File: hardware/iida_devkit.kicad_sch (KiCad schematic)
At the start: 4 parts

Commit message: HW: Refine schematic
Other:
- sheet Power ports: added V_3V3, V_BAT; removed +3.3V, V_{BAT}
- note added: "This is a project for practicing PCB design and programming. The result is a device that is powered either with a battery or with a USB connection. The device can recharge the battery via the USB connection. The device includes: - An example sensor (temperature) - External flash for updating the firmware over the air (FOTA) - A modem module that connects the main microcontroller to the internet w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"
- note removed: "This is a project for practicing PCB design and programming. The result is a device that is powered either with a battery or with a USB connection. The device can recharge the batteries via the USB connection. The device includes: - An example sensor (temperature) - External flash for updating the firmware over the air (FOTA) - A modem module that connects the main microcontroller to the internet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"
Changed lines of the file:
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@@
+	(wire
+		(pts
+			(xy 151.13 105.41) (xy 142.24 105.41)
+		)
+		(stroke
+			(width 0)
+			(type default)
+		)
+	)
 	(wire
 		(pts
@@
 	(wire
 		(pts
-			(xy 142.24 105.41) (xy 149.86 105.41)
-		)
-		(stroke
-			(width 0)
-			(type default)
-		)
-	)
-	(wire
-		(pts
 			(xy 142.24 102.87) (xy 144.78 102.87)
 		)
@@
 		(pts
 			(xy 118.11 128.27) (xy 124.46 128.27)
+		)
+		(stroke
+			(width 0)
+			(type default)
+		)
+	)
+	(wire
+		(pts
+			(xy 151.13 102.87) (xy 151.13 105.41)
 		)
 		(stroke
@@
 		)
 	)
-	(text "This is a project for practicing PCB design and programming.\n\nThe result is a device that is powered either with a battery or with a USB connection.\nThe device can recharge the batteries via the USB connection.\n\nThe device includes:\n  - An example sensor (temperature)\n  - External flash for updating the firmware over the air (FOTA)\n  - A modem module that connects the main microcontroller to the internet with LTE CAT-M1\n  - Option to use either an external antenna or an integrated antenna\n\nA key goal of the project is to ensure it has as little reliance as possible on totalitarian\ncountries like China or Russia.\nComponent sourcing must be done carefully to select manufacturers who can supply parts that are not\nproduced in such countries.\nInstead, democratic countries such as Taiwan and Germany should be preferred.\n\nTo reduce strain on the global environment, manufacturing and sourcing is centered around Europe."
+	(text "This is a project for practicing PCB design and programming.\n\nThe result is a device that is powered either with a battery or with a USB connection.\nThe device can recharge the battery via the USB connection.\n\nThe device includes:\n  - An example sensor (temperature)\n  - External flash for updating the firmware over the air (FOTA)\n  - A modem module that connects the main microcontroller to the internet with LTE CAT-M1\n  - Option to use either an external antenna or an integrated antenna\n\nA key goal of the project is to ensure it has as little reliance as possible on totalitarian\ncountries (e.g., China or Russia) or on hostile countries (e.g., USA).\nComponent sourcing must be done carefully to select manufacturers who can supply parts that are not\nproduced in such countries.\nInstead, democratic countries (e.g., Taiwan and Germany) should be preferred.\n\nTo reduce strain on the global environment, manufacturing and sourcing is centered around Europe."
 		(exclude_from_sim no)
 		(at 14.478 52.07 0)
@@
 		(dnp no)
 		(fields_autoplaced yes)
-		(property "Reference" "#PWR03"
+		(property "Reference" "#PWR02"
 			(at 149.86 198.12 0)
 			(effects
@@
 			(project "iida_devkit"
 				(path "/b12a6e25-97fb-4aba-bc96-af8db389bb9a"
-					(reference "#PWR03")
+					(reference "#PWR02")
+					(unit 1)
+				)
+			)
+		)
+	)
+	(symbol
+		(lib_id "power:+3.3V")
+		(at 144.78 102.87 0)
+		(unit 1)
+		(exclude_from_sim no)
+		(in_bom yes)
+		(on_board yes)
+		(dnp no)
+		(property "Reference" "#PWR01"
+			(at 144.78 106.68 0)
+			(effects
+				(font
+					(size 1.27 1.27)
+				)
+				(hide yes)
+			)
+		)
+		(property "Value" "V_3V3"
+			(at 144.78 99.314 0)
+			(effects
+				(font
+					(size 1.27 1.27)
+				)
+			)
+		)
+		(property "Footprint" ""
+			(at 144.78 102.87 0)
+			(effects
+				(font
+					(size 1.27 1.27)
+				)
+				(hide yes)
+			)
+		)
+		(property "Datasheet" ""
+			(at 144.78 102.87 0)
+			(effects
+				(font
+					(size 1.27 1.27)
+				)
+				(hide yes)
+			)
+		)
+		(property "Description" "Power symbol creates a global label with name \"+3.3V\""
+			(at 144.78 102.87 0)
+			(effects
+				(font
+					(size 1.27 1.27)
+				)
+				(hide yes)
+			)
+		)
+		(pin "1"
+		)
+		(instances
+			(project "iida_devkit"
+				(path "/b12a6e25-97fb-4aba-bc96-af8db389bb9a"
+					(reference "#PWR01")
 					(unit 1)
 				)
@@
 	(symbol
 		(lib_id "power:+BATT")
-		(at 149.86 105.41 0)
+		(at 151.13 102.87 0)
 		(unit 1)
 		(exclude_from_sim no)
@@
 		(on_board yes)
 		(dnp no)
-		(property "Reference" "#PWR02"
-			(at 149.86 109.22 0)
-			(effects
-				(font
-					(size 1.27 1.27)
-				)
-				(hide yes)
-			)
-		)
-		(property "Value" "+VBAT"
-			(at 149.86 101.854 0)
+		(property "Reference" "#PWR03"
+			(at 151.13 106.68 0)
+			(effects
+				(font
+					(size 1.27 1.27)
+				)
+				(hide yes)
+			)
+		)
+		(property "Value" "V_BAT"
+			(at 151.13 99.314 0)
 			(effects
 				(font
@@
 		)
 		(property "Footprint" ""
-			(at 149.86 105.41 0)
+			(at 151.13 102.87 0)
 			(effects
 				(font
@@
 		)
 		(property "Datasheet" ""
-			(at 149.86 105.41 0)
+			(at 151.13 102.87 0)
 			(effects
 				(font
@@
 		)
 		(property "Description" "Power symbol creates a global label with name \"+BATT\""
-			(at 149.86 105.41 0)
+			(at 151.13 102.87 0)
 			(effects
 				(font
@@
 			(project "iida_devkit"
 				(path "/b12a6e25-97fb-4aba-bc96-af8db389bb9a"
-					(reference "#PWR02")
-					(unit 1)
-				)
-			)
-		)
-	)
-	(symbol
-		(lib_id "power:+3.3V")
-		(at 144.78 102.87 0)
-		(unit 1)
-		(exclude_from_sim no)
-		(in_bom yes)
-		(on_board yes)
-		(dnp no)
-		(property "Reference" "#PWR01"
-			(at 144.78 106.68 0)
-			(effects
-				(font
-					(size 1.27 1.27)
-				)
-				(hide yes)
-			)
-		)
-		(property "Value" "+3.3V"
-			(at 144.78 99.06 0)
-			(effects
-				(font
-					(size 1.27 1.27)
-				)
-			)
-		)
-		(property "Footprint" ""
-			(at 144.78 102.87 0)
-			(effects
-				(font
-					(size 1.27 1.27)
-				)
-				(hide yes)
-			)
-		)
-		(property "Datasheet" ""
-			(at 144.78 102.87 0)
-			(effects
-				(font
-					(size 1.27 1.27)
-				)
-				(hide yes)
-			)
-		)
-		(property "Description" "Power symbol creates a global label with name \"+3.3V\""
-			(at 144.78 102.87 0)
-			(effects
-				(font
-					(size 1.27 1.27)
-				)
-				(hide yes)
-			)
-		)
-		(pin "1"
-		)
-		(instances
-			(project "iida_devkit"
-				(path "/b12a6e25-97fb-4aba-bc96-af8db389bb9a"
-					(reference "#PWR01")
+					(reference "#PWR03")
 					(unit 1)
 				)
@@
 			)
 		)
-		(pin "V_{BAT}" output
+		(pin "V_BAT" output
 			(at 142.24 105.41 0)
 			(effects
@@
 			)
 		)
-		(pin "+3.3V" output
+		(pin "V_3V3" output
 			(at 142.24 102.87 0)
 			(effects

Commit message: HW: Start working on Hw v5.0.0
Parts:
- H1, H2, H3, H4: Digi-Key Part Number - -> (none)
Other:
- added sheet Antenna (antenna.kicad_sch)
- added sheet Battery (battery.kicad_sch)
- added sheet USB (usb.kicad_sch)
- sheet MCU ports: added MDM_PWR_EN, MDM_PWR_ON, MDM_RESET, MDM_RXD, MDM_TXD, V_BAT; removed MODEM_PWR_ENn, MODEM_RESET, MODEM_RX, MODEM_TX
- sheet Modem ports: added ANT, MDM_PWR_EN, MDM_PWR_ON, MDM_RESET, MDM_RXD, MDM_TXD, MDM_V_INT, SIM_DET, SIM_VCC; removed MODEM_PWR_ENn, MODEM_RESET, MODEM_RX, MODEM_TX, VSIM
- sheet Power ports: added V_5V0; removed USB_DN, USB_DP
- sheet SIM ports: added MDM_V_INT, SIM_DET, SIM_VCC; removed VSIM

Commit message: HW: Refine schematic
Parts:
- H1, H2, H3, H4: footprint MountingHole:MountingHole_2.2mm_M2_Pad_Via -> MountingHole:MountingHole_5.3mm_M5_Pad_Via
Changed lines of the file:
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@@
 			)
 		)
-		(property "Footprint" "MountingHole:MountingHole_2.2mm_M2_Pad_Via"
+		(property "Footprint" "MountingHole:MountingHole_5.3mm_M5_Pad_Via"
 			(at 134.62 189.23 0)
 			(effects
@@
 			)
 		)
-		(property "Footprint" "MountingHole:MountingHole_2.2mm_M2_Pad_Via"
+		(property "Footprint" "MountingHole:MountingHole_5.3mm_M5_Pad_Via"
 			(at 149.86 189.23 0)
 			(effects
@@
 			)
 		)
-		(property "Footprint" "MountingHole:MountingHole_2.2mm_M2_Pad_Via"
+		(property "Footprint" "MountingHole:MountingHole_5.3mm_M5_Pad_Via"
 			(at 139.7 189.23 0)
 			(effects
@@
 			)
 		)
-		(property "Footprint" "MountingHole:MountingHole_2.2mm_M2_Pad_Via"
+		(property "Footprint" "MountingHole:MountingHole_5.3mm_M5_Pad_Via"
 			(at 144.78 189.23 0)
 			(effects

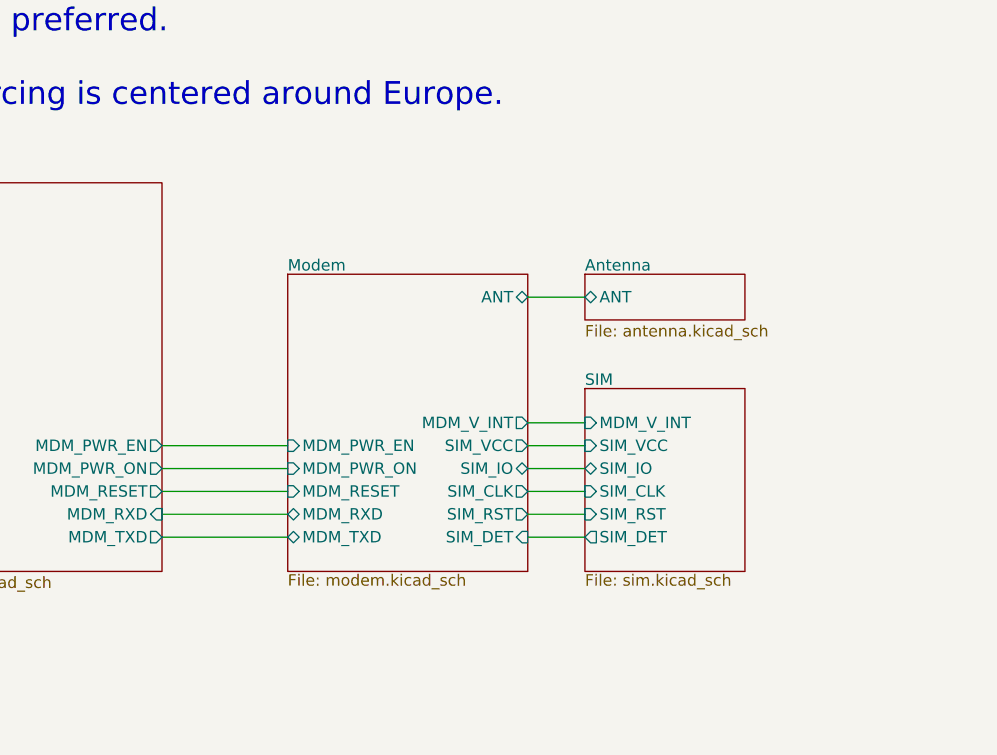
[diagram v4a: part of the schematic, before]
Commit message: HW: Fill BOM and refine schema
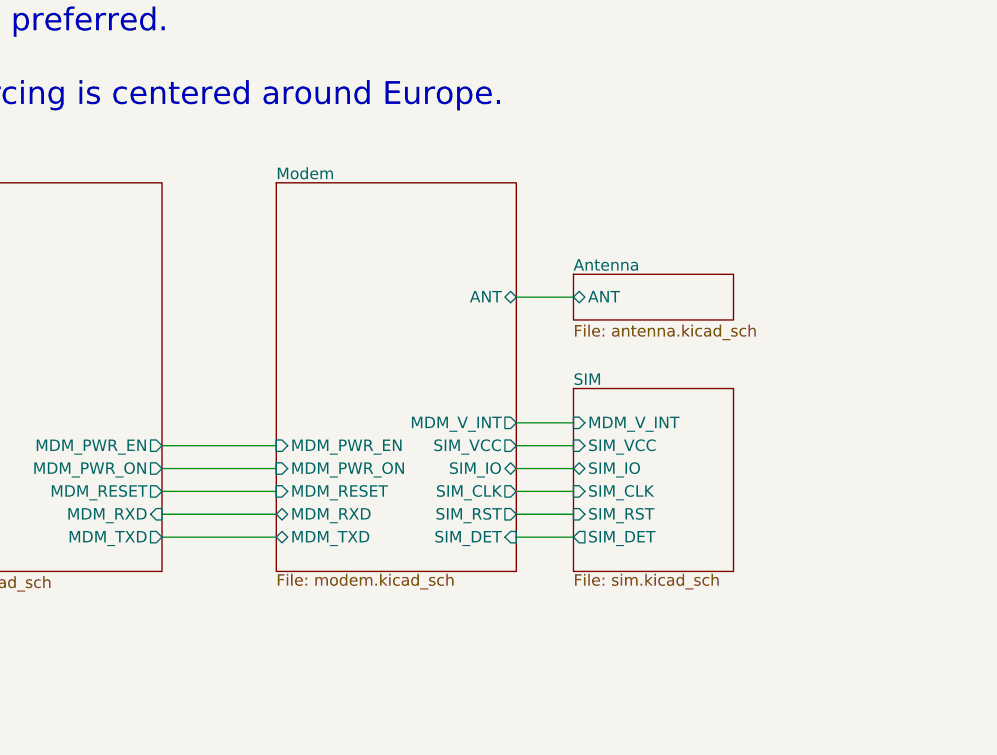
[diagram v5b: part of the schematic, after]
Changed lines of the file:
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@@
 	(wire
 		(pts
-			(xy 193.04 128.27) (xy 199.39 128.27)
-		)
-		(stroke
-			(width 0)
-			(type default)
-		)
-	)
-	(wire
-		(pts
-			(xy 193.04 135.89) (xy 199.39 135.89)
-		)
-		(stroke
-			(width 0)
-			(type default)
-		)
-	)
-	(wire
-		(pts
-			(xy 152.4 133.35) (xy 166.37 133.35)
+			(xy 191.77 128.27) (xy 198.12 128.27)
+		)
+		(stroke
+			(width 0)
+			(type default)
+		)
+	)
+	(wire
+		(pts
+			(xy 191.77 135.89) (xy 198.12 135.89)
+		)
+		(stroke
+			(width 0)
+			(type default)
+		)
+	)
+	(wire
+		(pts
+			(xy 152.4 133.35) (xy 165.1 133.35)
 		)
 		(stroke
@@
 	(wire
 		(pts
-			(xy 152.4 130.81) (xy 166.37 130.81)
-		)
-		(stroke
-			(width 0)
-			(type default)
-		)
-	)
-	(wire
-		(pts
-			(xy 193.04 133.35) (xy 199.39 133.35)
+			(xy 152.4 130.81) (xy 165.1 130.81)
+		)
+		(stroke
+			(width 0)
+			(type default)
+		)
+	)
+	(wire
+		(pts
+			(xy 191.77 133.35) (xy 198.12 133.35)
 		)
 		(stroke
@@
 	(wire
 		(pts
-			(xy 193.04 123.19) (xy 199.39 123.19)
+			(xy 191.77 123.19) (xy 198.12 123.19)
 		)
 		(stroke
@@
 	(wire
 		(pts
-			(xy 193.04 109.22) (xy 199.39 109.22)
-		)
-		(stroke
-			(width 0)
-			(type default)
-		)
-	)
-	(wire
-		(pts
-			(xy 193.04 130.81) (xy 199.39 130.81)
+			(xy 191.77 109.22) (xy 198.12 109.22)
+		)
+		(stroke
+			(width 0)
+			(type default)
+		)
+	)
+	(wire
+		(pts
+			(xy 191.77 130.81) (xy 198.12 130.81)
 		)
 		(stroke
@@
 	(wire
 		(pts
-			(xy 152.4 128.27) (xy 166.37 128.27)
+			(xy 152.4 128.27) (xy 165.1 128.27)
 		)
 		(stroke
@@
 	(wire
 		(pts
-			(xy 152.4 125.73) (xy 166.37 125.73)
+			(xy 152.4 125.73) (xy 165.1 125.73)
 		)
 		(stroke
@@
 	(wire
 		(pts
-			(xy 152.4 135.89) (xy 166.37 135.89)
-		)
-		(stroke
-			(width 0)
-			(type default)
-		)
-	)
-	(wire
-		(pts
-			(xy 193.04 125.73) (xy 199.39 125.73)
+			(xy 152.4 135.89) (xy 165.1 135.89)
+		)
+		(stroke
+			(width 0)
+			(type default)
+		)
+	)
+	(wire
+		(pts
+			(xy 191.77 125.73) (xy 198.12 125.73)
 		)
 		(stroke
@@
 			)
 		)
+		(property "Power" ""
+			(at 134.62 189.23 0)
+			(effects
+				(font
+					(size 1.27 1.27)
+				)
+				(hide yes)
+			)
+		)
 		(pin "1"
 		)
@@
 		)
 		(property "MPN" "-"
+			(at 149.86 189.23 0)
+			(effects
+				(font
+					(size 1.27 1.27)
+				)
+				(hide yes)
+			)
+		)
+		(property "Power" ""
 			(at 149.86 189.23 0)
 			(effects
@@
 			)
 		)
+		(property "Power" ""
+			(at 139.7 189.23 0)
+			(effects
+				(font
+					(size 1.27 1.27)
+				)
+				(hide yes)
+			)
+		)
 		(pin "1"
 		)
@@
 			)
 		)
+		(property "Power" ""
+			(at 144.78 189.23 0)
+			(effects
+				(font
+					(size 1.27 1.27)
+				)
+				(hide yes)
+			)
+		)
 		(pin "1"
 		)
@@
 	)
 	(sheet
-		(at 199.39 119.38)
+		(at 198.12 119.38)
 		(size 17.78 20.32)
 		(exclude_from_sim no)
@@
 		)
 		(property "Sheetname" "SIM"
-			(at 199.39 119.126 0)
+			(at 198.12 119.126 0)
 			(effects
 				(font
@@
 		)
 		(property "Sheetfile" "sim.kicad_sch"
-			(at 199.39 139.954 0)
+			(at 198.12 139.954 0)
 			(effects
 				(font
@@
 		)
 		(pin "MDM_V_INT" input
-			(at 199.39 123.19 180)
+			(at 198.12 123.19 180)
 			(effects
 				(font
@@
 		)
 		(pin "SIM_CLK" input
-			(at 199.39 130.81 180)
+			(at 198.12 130.81 180)
 			(effects
 				(font
@@
 		)
 		(pin "SIM_DET" output
-			(at 199.39 135.89 180)
+			(at 198.12 135.89 180)
 			(effects
 				(font
@@
 		)
 		(pin "SIM_IO" bidirectional
-			(at 199.39 128.27 180)
+			(at 198.12 128.27 180)
 			(effects
 				(font
@@
 		)
 		(pin "SIM_RST" input
-			(at 199.39 133.35 180)
+			(at 198.12 133.35 180)
 			(effects
 				(font
@@
 		)
 		(pin "SIM_VCC" input
-			(at 199.39 125.73 180)
+			(at 198.12 125.73 180)
 			(effects
 				(font
@@
 	)
 	(sheet
-		(at 166.37 106.68)
-		(size 26.67 33.02)
+		(at 165.1 96.52)
+		(size 26.67 43.18)
 		(exclude_from_sim no)
 		(in_bom yes)
@@
 		)
 		(property "Sheetname" "Modem"
-			(at 166.37 106.426 0)
+			(at 165.1 96.266 0)
 			(effects
 				(font
@@
 		)
 		(property "Sheetfile" "modem.kicad_sch"
-			(at 166.37 139.954 0)
+			(at 165.1 139.954 0)
 			(effects
 				(font
@@
 		)
 		(pin "ANT" bidirectional
-			(at 193.04 109.22 0)
+			(at 191.77 109.22 0)
 			(effects
 				(font
@@
 		)
 		(pin "MDM_PWR_EN" input
-			(at 166.37 125.73 180)
+			(at 165.1 125.73 180)
 			(effects
 				(font
@@
 		)
 		(pin "MDM_PWR_ON" input
-			(at 166.37 128.27 180)
+			(at 165.1 128.27 180)
 			(effects
 				(font
@@
 		)
 		(pin "MDM_RESET" input
-			(at 166.37 130.81 180)
+			(at 165.1 130.81 180)
 			(effects
 				(font
@@
 		)
 		(pin "MDM_RXD" bidirectional
-			(at 166.37 133.35 180)
+			(at 165.1 133.35 180)
 			(effects
 				(font
@@
 		)
 		(pin "MDM_TXD" bidirectional
-			(at 166.37 135.89 180)
+			(at 165.1 135.89 180)
 			(effects
 				(font
@@
 		)
 		(pin "MDM_V_INT" output
-			(at 193.04 123.19 0)
+			(at 191.77 123.19 0)
 			(effects
 				(font
@@
 		)
 		(pin "SIM_CLK" output
-			(at 193.04 130.81 0)
+			(at 191.77 130.81 0)
 			(effects
 				(font
@@
 		)
 		(pin "SIM_DET" input
-			(at 193.04 135.89 0)
+			(at 191.77 135.89 0)
 			(effects
 				(font
@@
 		)
 		(pin "SIM_IO" bidirectional
-			(at 193.04 128.27 0)
+			(at 191.77 128.27 0)
 			(effects
 				(font
@@
 		)
 		(pin "SIM_RST" output
-			(at 193.04 133.35 0)
+			(at 191.77 133.35 0)
 			(effects
 				(font
@@
 		)
 		(pin "SIM_VCC" output
-			(at 193.04 125.73 0)
+			(at 191.77 125.73 0)
 			(effects
 				(font
@@
 	)
 	(sheet
-		(at 199.39 106.68)
+		(at 198.12 106.68)
 		(size 17.78 5.08)
 		(exclude_from_sim no)
@@
 		)
 		(property "Sheetname" "Antenna"
-			(at 199.39 106.426 0)
+			(at 198.12 106.426 0)
 			(effects
 				(font
@@
 		)
 		(property "Sheetfile" "antenna.kicad_sch"
-			(at 199.39 112.268 0)
+			(at 198.12 112.268 0)
 			(effects
 				(font
@@
 		)
 		(pin "ANT" bidirectional
-			(at 199.39 109.22 180)
-			(effects
-				(font
+			(at 198.12 109.22 180)
+			(effects
+				(font

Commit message: HW: Section schematics
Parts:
- added FID1, FID2, FID3: Fiducial, Fiducial:Fiducial_1mm_Mask2mm, symbol Mechanical:Fiducial
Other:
- sheet MCU ports: added MDM_CTS, MDM_RTS; removed none
- sheet Modem ports: added MDM_CTS, MDM_RTS; removed none
- note added: "Place a stitched GND guard rail around the edges of the PCB to provide a grounding point for human touch."
- note added: "Place fiducials on three corners of the PCB."
- moved on the sheet: H1, H2, H3, H4
